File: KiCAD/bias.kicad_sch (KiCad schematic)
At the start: 23 parts, among them Q2 2N7000, Q3 2N7000, U10 OPA454, U11 LM4040LP-5, U5 OPA454, U9 LM7805_TO220

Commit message: kicad(bias): swap C17/C18 from Device:C_Polarized to Device:C
1 uF X7R ceramic is non-polarized in production. The polarized symbol
was an assembly-orientation hazard for a part that doesn't actually
have polarity. Pin numbers and connections unchanged.

- lib_id Device:C_Polarized -> Device:C on both caps
- Description property "Polarized capacitor" -> "Unpolarized capacitor"
- grid_bias.md: update note and check off the open-item

Co-Authored-By: Claude Opus 4.7 <noreply@anthropic.com>
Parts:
- C17, C18: symbol Device:C_Polarized -> Device:C
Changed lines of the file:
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@@
 	)
 	(symbol
-		(lib_id "Device:C_Polarized")
+		(lib_id "Device:C")
 		(at 107.95 163.83 0)
 		(unit 1)
@@
 			)
 		)
-		(property "Description" "Polarized capacitor"
+		(property "Description" "Unpolarized capacitor"
 			(at 107.95 163.83 0)
 			(hide yes)
@@
 	)
 	(symbol
-		(lib_id "Device:C_Polarized")
+		(lib_id "Device:C")
 		(at 107.95 185.42 0)
 		(unit 1)
@@
 			)
 		)
-		(property "Description" "Polarized capacitor"
+		(property "Description" "Unpolarized capacitor"
 			(at 107.95 185.42 0)
 			(hide yes)

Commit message: kicad: assign 1/4 W metal-film through-hole footprint to all resistors
Footprint: Resistor_THT:R_Axial_DIN0207_L6.3mm_D2.5mm_P10.16mm_Horizontal

DIN 0207 is the standard 1/4 W metal-film body size (Vishay MRS25, Yageo
MFR-25, etc., 6.3 mm x 2.5 mm). The relaxed P10.16mm pitch (vs the snug
P7.62mm) gives extra lead-bend room for hand soldering.

- bias.kicad_sch: 10 resistors (R_FA, R_FB, R_GA, R_GB, R_GATE, R_GLA,
  R_GLB, R_PADA, R_PADB, R_Z)
- buffer_keyer.kicad_sch: 25 resistors (R1-R16, RF_OP, RF_OP1, RG_OP,
  RG_OP1, RLA, RLB, R_INJ1, R_INJ2, Re)

All values fit comfortably in the DIN 0207 body, including the three
51-ohm MC1496 emitter resistors (1 % metal film for carrier-null
precision) and the 330 k MCP4728 null-injection isolators.

Co-Authored-By: Claude Opus 4.7 <noreply@anthropic.com>
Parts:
- R_FA, R_FB, R_GA, R_GATE, R_GB, R_GLA, R_GLB, R_PADA, R_PADB, R_Z: footprint (none) -> Resistor_THT:R_Axial_DIN0207_L6.3mm_D2.5mm_P10.16mm_Horizontal
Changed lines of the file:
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@@
 			)
 		)
-		(property "Footprint" ""
+		(property "Footprint" "Resistor_THT:R_Axial_DIN0207_L6.3mm_D2.5mm_P10.16mm_Horizontal"
 			(at 72.644 77.724 90)
 			(hide yes)
@@
 			)
 		)
-		(property "Footprint" ""
+		(property "Footprint" "Resistor_THT:R_Axial_DIN0207_L6.3mm_D2.5mm_P10.16mm_Horizontal"
 			(at 73.914 85.344 90)
 			(hide yes)
@@
 			)
 		)
-		(property "Footprint" ""
+		(property "Footprint" "Resistor_THT:R_Axial_DIN0207_L6.3mm_D2.5mm_P10.16mm_Horizontal"
 			(at 105.664 120.904 90)
 			(hide yes)
@@
 			)
 		)
-		(property "Footprint" ""
+		(property "Footprint" "Resistor_THT:R_Axial_DIN0207_L6.3mm_D2.5mm_P10.16mm_Horizontal"
 			(at 71.374 124.714 90)
 			(hide yes)
@@
 			)
 		)
-		(property "Footprint" ""
+		(property "Footprint" "Resistor_THT:R_Axial_DIN0207_L6.3mm_D2.5mm_P10.16mm_Horizontal"
 			(at 105.664 81.534 90)
 			(hide yes)
@@
 			)
 		)
-		(property "Footprint" ""
+		(property "Footprint" "Resistor_THT:R_Axial_DIN0207_L6.3mm_D2.5mm_P10.16mm_Horizontal"
 			(at 89.154 68.834 90)
 			(hide yes)
@@
 			)
 		)
-		(property "Footprint" ""
+		(property "Footprint" "Resistor_THT:R_Axial_DIN0207_L6.3mm_D2.5mm_P10.16mm_Horizontal"
 			(at 92.964 108.204 90)
 			(hide yes)
@@
 			)
 		)
-		(property "Footprint" ""
+		(property "Footprint" "Resistor_THT:R_Axial_DIN0207_L6.3mm_D2.5mm_P10.16mm_Horizontal"
 			(at 54.864 131.064 90)
 			(hide yes)
@@
 			)
 		)
-		(property "Footprint" ""
+		(property "Footprint" "Resistor_THT:R_Axial_DIN0207_L6.3mm_D2.5mm_P10.16mm_Horizontal"
 			(at 39.116 114.554 90)
 			(hide yes)
@@
 			)
 		)
-		(property "Footprint" ""
+		(property "Footprint" "Resistor_THT:R_Axial_DIN0207_L6.3mm_D2.5mm_P10.16mm_Horizontal"
 			(at 77.724 117.094 90)
 			(hide yes)

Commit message: docs+kicad+qucs: lock in cathode-monitor diode-OR design
KiCad bias sheet: fill in placeholder R values for the cathode-monitor
section -- R18=10K (threshold divider bottom), R20=R22=7.5K (R_SOURCE,
one per channel), R21=R23=470K (R_HYST, one per channel). All cathode-
monitor resistors now match the QUCS test bench values.

QUCS grid_bias_check.sch: rebuild test bench with LM393-equivalent
behavioral comparator (gain 1e4 to avoid the 1e6 convergence trap),
R_HYST=470K, R_SOURCE=7.5K, sweep input V2 against threshold V3=1.0V.
Sweep crosses the trip point cleanly with the lower gain.

pa_cathode_monitor.md: lock in the diode-OR combiner topology (no
inverter) chosen this session. Corrects the prior wired-OR description
which had the wrong polarity for an OC-direct-tie scheme. Updates:
  - Level 5 table: add R_SOURCE row, mark R_PULLUP as per-channel
  - Level 5 narrative: corrects input polarity (V_sense on +, threshold
    on -, fault=HIGH) and timing budget
  - Threshold divider: R17/RV1/R18 = 27K/10K/10K giving 1.06-2.13V
    wiper range (was an older 4.7K/1K/1.5K plan)
  - Per-tube summing: explicit diode-OR diagram with rationale for why
    a naive wired-tie gives wired-AND-of-fault instead of OR
  - Watchdog gate: replace stale screen-voltage interrupter section
    with grid-bias slam (Q2/Q3 on bias sheet) pointer
  - BOM: updated to match
  - Open items: latch decision resolved; new items track diode-OR
    parts (D_OR_A/B, R_PD) and I_CATHODE_A/B labels still to add

Add 1N5817 and Bourns 3296W trim-pot datasheets used for these decisions.

Co-Authored-By: Claude Opus 4.7 <noreply@anthropic.com>
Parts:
- added C24, C27, C31: 100nF, symbol Device:C
- added C25, C26, C30: 10uF, symbol Device:C_Polarized
- added C28, C29: 1nF, symbol Device:C
- added D1, D2, D3, D4: 1N5817, Diode_THT:D_DO-41_SOD81_P10.16mm_Horizontal, symbol Diode:1N5817
- added R17: 27K, symbol Device:R_US
- added R18: 10K, symbol Device:R_US
- added R19: 4.7K, symbol Device:R_US
- added R20, R22: 7.5K, symbol Device:R_US
- added R21, R23: 470K, symbol Device:R_US
- added RV1: 10K, symbol Device:R_Potentiometer_US
- added U12: LM393, symbol Comparator:LM393
- added U13, U14: OPA1641, symbol Amplifier_Operational:OPA1641
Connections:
- net +5V: now also C24.1, C25.1, C26.1, C27.1, C30.1, C31.1, U12.8 (V+), U13.7 (V+), U14.7 (V+)
- net GND: now also C24.2, C25.2, C26.2, C27.2, C28.2, C29.2, C30.2, C31.2, D1.2 (A), D3.2 (A), R18.2, U12.4 (V-), U13.4 (V-), U14.4 (V-)
- net GRID_BLOCK_CRASH: now also R19.2, R21.2, R23.2, U12.1, U12.7
- net +5V_REF: now reaches C23.1, R_GA.1, R_GB.1, R_Z.2, U11.2 (K)
- net +5V_REF: now also R17.1
- new net: R18.1, RV1.3
- new net: R20.1, U13.2 (-), U13.6
- new net: R20.2, R21.1, U12.5 (+)
- new net: R22.1, U14.2 (-), U14.6
- new net: R22.2, R23.1, U12.3 (+)
- new net: R17.2, RV1.1
- new net: RV1.2, U12.2 (-), U12.6 (-)
- new net +3.3V: D2.1 (K), D4.1 (K), R19.1
- new net CATHODE_SENSE_A: C29.1, D3.1 (K), D4.2 (A), U14.3 (+)
- new net CATHODE_SENSE_B: C28.1, D1.1 (K), D2.2 (A), U13.3 (+)

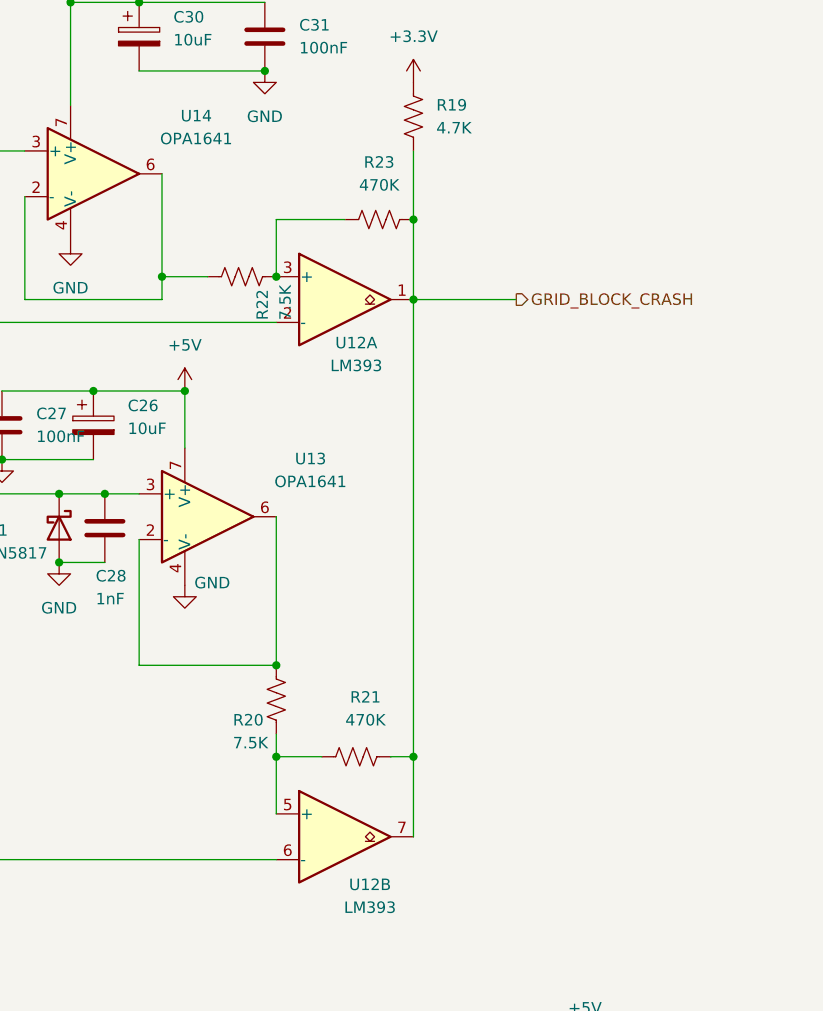
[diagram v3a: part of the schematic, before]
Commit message: kicad+pdf+tools: diode-OR build-out, cap footprints, regen monitor PDF
KiCad bias sheet: complete the cathode-monitor diode-OR combiner
  - D5, D6 = 1N4148 (diode-OR anodes at each LM393 OC output)
  - R24 = 100 kOhm (R_PD pulldown at common GRID_BLOCK_CRASH node)
  - R25 = 4.7 kOhm (second R_PULL so each LM393 OC has its own
    pull-up to +3.3 V, satisfying the diode-OR topology)
  - Closes the "remaining bias-sheet work" item from the cathode-
    monitor spec's open list.

KiCad arduino sheet: add I_CATHODE_A and I_CATHODE_B hierarchical
inputs so the ADC1 path from the bias sheet has a landing point on
the Metro side.

Tools: add assign_cap_footprints.py, a re-runnable script that walks
.kicad_sch files and assigns THT capacitor footprints by value, based
on the parts on the 2026-06-19 Mouser order:
  100nF / 0.1uF  KEMET C410   C_Disc_D5.0mm_W2.5mm_P5.00mm
  10uF           Panasonic    CP_Radial_D5.0mm_P2.00mm
  680nF / 0.68uF WIMA MKP4    C_Rect_L13.0mm_W6.0mm_P10.00mm_FKS3_FKP3_MKS4
  10nF / 0.01uF  Vishay Y5P   C_Disc_D6.0mm_W2.5mm_P5.00mm
  220pF          Knowles mica C_Rect_L7.0mm_W4.5mm_P5.00mm
Only fills empty Footprint fields; never overwrites. Preserves LF
line endings and writes UTF-8 without BOM (KiCad 10 treats a BOM-
prefixed .kicad_sch as empty).

Run output: 10 caps updated on bias sheet, 17 on buffer_keyer sheet.
Values still needing the user to measure (not in this order):
  bias: C17/C18 1uF, C21 0.22uF, C28/C29 1nF
  buffer_keyer: C1 330pF, C13/C14/C15 1uF
  vfo: CF3/CF5 390pF

Cathode_Monitor_Schematic.pdf regenerated with the diode-OR topology
locked in:
  - Schematic page adds L5b diode-OR sub-diagram (D_OR_A horizontal,
    D_OR_B from "Ch. B" annotation, R_PD pulldown, GRID_BLOCK_CRASH
    output)
  - R_SOURCE now drawn explicitly between OPA1641 OUT and LM393 (+)
  - V_REF block replaced with V_THR (R17/RV1/R18 trim, 1.06-2.13 V)
  - BOM, layers table, operating-points action column updated
  - "Watchdog gate" section rewritten: bias s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
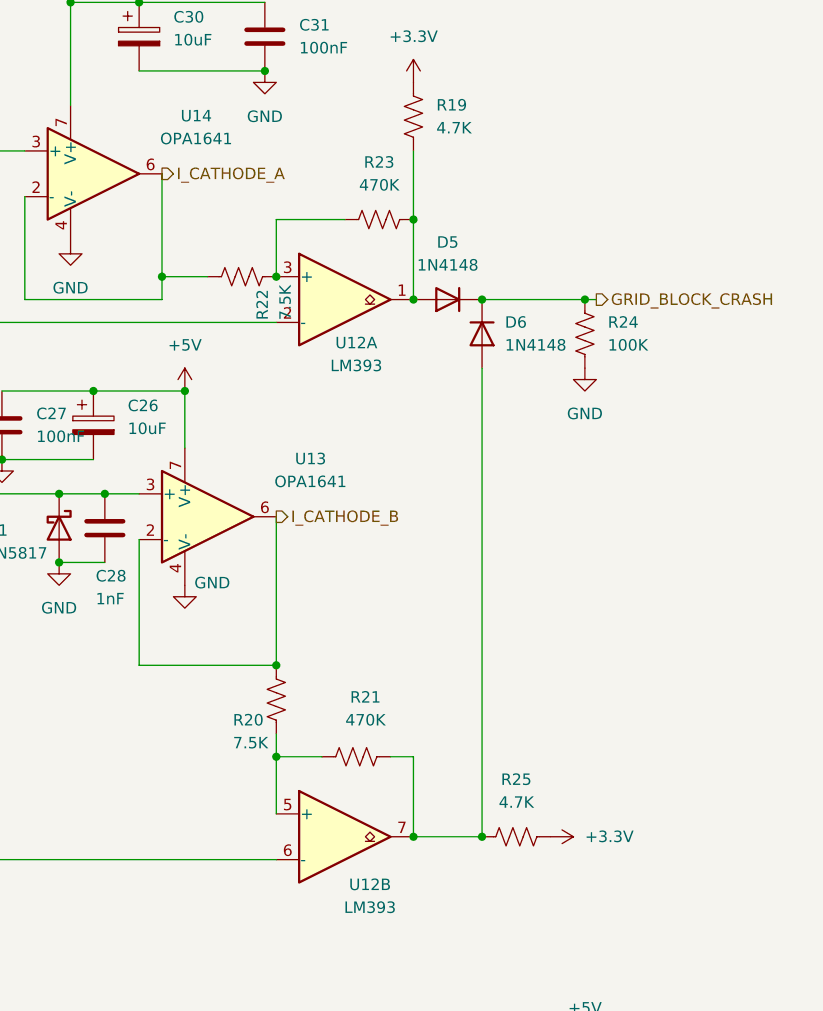
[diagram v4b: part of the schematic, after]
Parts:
- added D5, D6: 1N4148, Diode_THT:D_DO-35_SOD27_P7.62mm_Horizontal, symbol Diode:1N4148
- added R24: 100K, symbol Device:R_US
- added R25: 4.7K, symbol Device:R_US
- C19, C20, C22, C23, C24, C27, C31: footprint (none) -> Capacitor_THT:C_Disc_D5.0mm_W2.5mm_P5.00mm
- C25, C26, C30: footprint (none) -> Capacitor_THT:CP_Radial_D5.0mm_P2.00mm
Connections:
- net +3.3V: now also R25.2
- net GND: now also R24.2
- net GRID_BLOCK_CRASH: now also D5.1 (K), D6.1 (K), R24.1; no longer R19.2, R21.2, R23.2, U12.1, U12.7
- net I_CATHODE_B: now reaches R20.1, U13.2 (-), U13.6
- net I_CATHODE_A: now reaches R22.1, U14.2 (-), U14.6
- new net: D5.2 (A), R19.2, R23.2, U12.1
- new net: D6.2 (A), R21.2, R25.1, U12.7

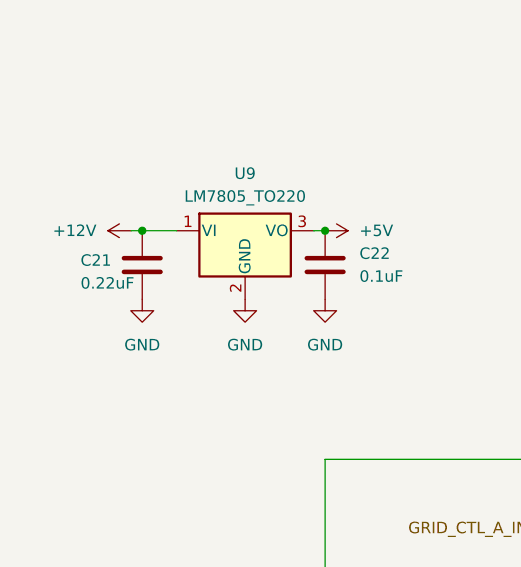
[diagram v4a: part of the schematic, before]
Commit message: caps: complete footprint coverage on active sheets + add datasheets
Pending Mouser cart 2026-06-24 (1:31 PM) adds two more KEMET parts
that close the remaining cap gaps:

  KEMET C317C334K3R5TA  0.33 uF X7R  25V  LS=5.08mm  (qty 4)
  KEMET C327C102J3G5TA  1000 pF C0G  25V  LS=5.08mm  (qty 5)

Updated VALUE_TO_FOOTPRINT and re-ran the script:
  bias: C21 0.33uF -> C_Rect_L7.0mm_W3.5mm_P5.00mm
  bias: C28/C29 1nF -> C_Rect_L7.0mm_W3.5mm_P5.00mm

Every capacitor across the active sheets (bias, buffer_keyer, vfo,
arduino) now has a footprint assigned. The 100pF (AVX AR21) mapping
remains for future PA tank / LPF use; no current schematic instance.

Also: Documentation/Components/ added for traceability of part choices:
  90968303_1-3748A_2026-06-19.pdf  -- Mouser invoice (R/Q/LM7171/DAC/etc)
  AR-Series.pdf                    -- AVX SkyCap/AR series MLCC
  C330C105K2R5TA.pdf               -- KEMET 1uF X7R 200V datasheet
  KEM_C1049_GOLDMAX_C0G.pdf        -- KEMET GoldMax C0G series
  KEM_C1050_GOLDMAX_X7R.pdf        -- KEMET GoldMax X7R series

Co-Authored-By: Claude Opus 4.7 <noreply@anthropic.com>
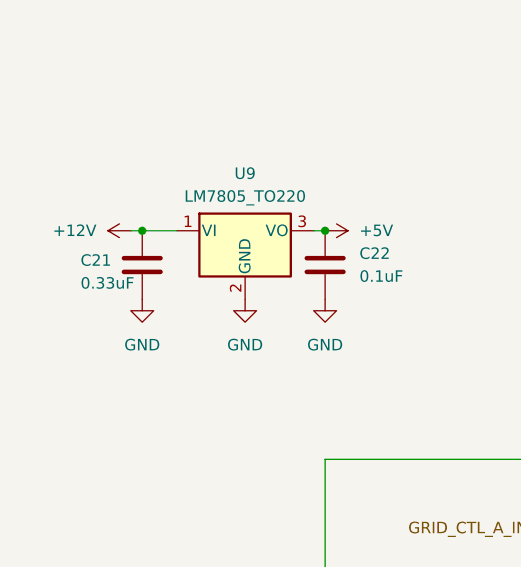
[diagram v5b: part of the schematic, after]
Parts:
- C17, C18: footprint (none) -> Capacitor_THT:C_Rect_L7.2mm_W4.5mm_P5.00mm
- C21: value 0.22uF -> 0.33uF; footprint (none) -> Capacitor_THT:C_Rect_L7.0mm_W3.5mm_P5.00mm
- C28, C29: footprint (none) -> Capacitor_THT:C_Rect_L7.0mm_W3.5mm_P5.00mm
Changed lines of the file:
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@@
 			)
 		)
-		(property "Value" "0.22uF"
+		(property "Value" "0.33uF"
 			(at 18.542 59.182 0)
 			(show_name no)
@@
 			)
 		)
-		(property "Footprint" ""
+		(property "Footprint" "Capacitor_THT:C_Rect_L7.0mm_W3.5mm_P5.00mm"
 			(at 26.3652 60.96 0)
 			(hide yes)
@@
 			)
 		)
-		(property "Footprint" ""
+		(property "Footprint" "Capacitor_THT:C_Rect_L7.2mm_W4.5mm_P5.00mm"
 			(at 108.9152 167.64 0)
 			(hide yes)
@@
 			)
 		)
-		(property "Footprint" ""
+		(property "Footprint" "Capacitor_THT:C_Rect_L7.0mm_W3.5mm_P5.00mm"
 			(at 205.4352 86.36 0)
 			(hide yes)
@@
 			)
 		)
-		(property "Footprint" ""
+		(property "Footprint" "Capacitor_THT:C_Rect_L7.2mm_W4.5mm_P5.00mm"
 			(at 108.9152 189.23 0)
 			(hide yes)
@@
 			)
 		)
-		(property "Footprint" ""
+		(property "Footprint" "Capacitor_THT:C_Rect_L7.0mm_W3.5mm_P5.00mm"
 			(at 190.1952 48.26 0)
 			(hide yes)

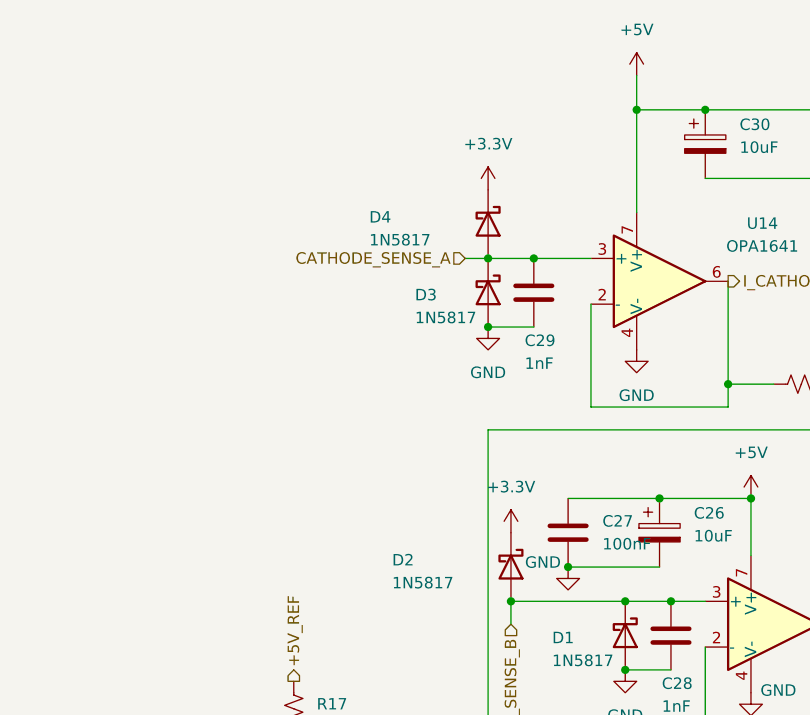
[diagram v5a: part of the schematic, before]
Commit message: kicad/bias: footprint cleanup -- D2/D4 +3.3V bulk + remaining cathode-monitor parts
User added two ECA-1EM100 10uF electrolytics for the D2/D4 fault-energy
absorption requirement, plus all the cathode-monitor section parts were
still missing footprints from when they were added.

Footprints assigned:
  C32, C33 -- 10uF (ECA-1EM100) -> CP_Radial_D5.0mm_P2.00mm
              (auto-assigned by assign_cap_footprints.py)
  R17-R25  -- 9x 1/4W metal-film -> R_Axial_DIN0207_L6.3mm_D2.5mm_P10.16mm_Horizontal
  RV1      -- 10K 25-turn cermet -> Potentiometer_Bourns_3296W_Vertical
  U12      -- LM393 dual comparator -> DIP-8_W7.62mm (Mill-Max 8P socket)
  U13, U14 -- OPA1641 -> DIP-8_W7.62mm (SOIC-to-DIP adapter into 8P socket)

C32 and C33 wiring verified:
  C32 (+ pin) -> +3.3V at (184.15, 33.02); (- pin) -> GND at (165.10, 33.02)
                 channel A, near D4 clamp
  C33 (+ pin) -> +3.3V at (186.69, 71.12); (- pin) -> GND at (175.26, 71.12)
                 channel B, near D2 clamp
Both polarized correctly for electrolytic; rail correctly identified as +3.3V.

Diode-OR wiring also verified:
  D5 anode (238.76, 57.15) = U12 ch A OC, cathode (246.38, 57.15) at common
  D6 anode (246.38, 64.77) connects to U12 ch B OC (238.76, 116.84) via long
           routing wire (south 52mm, then west 7.6mm)
  R19, R25 = per-channel 4.7K pull-ups to +3.3V
  R24 = 100K pull-down between common node and GND
  GRID_BLOCK_CRASH label tapped on the common node

Co-Authored-By: Claude Opus 4.7 <noreply@anthropic.com>
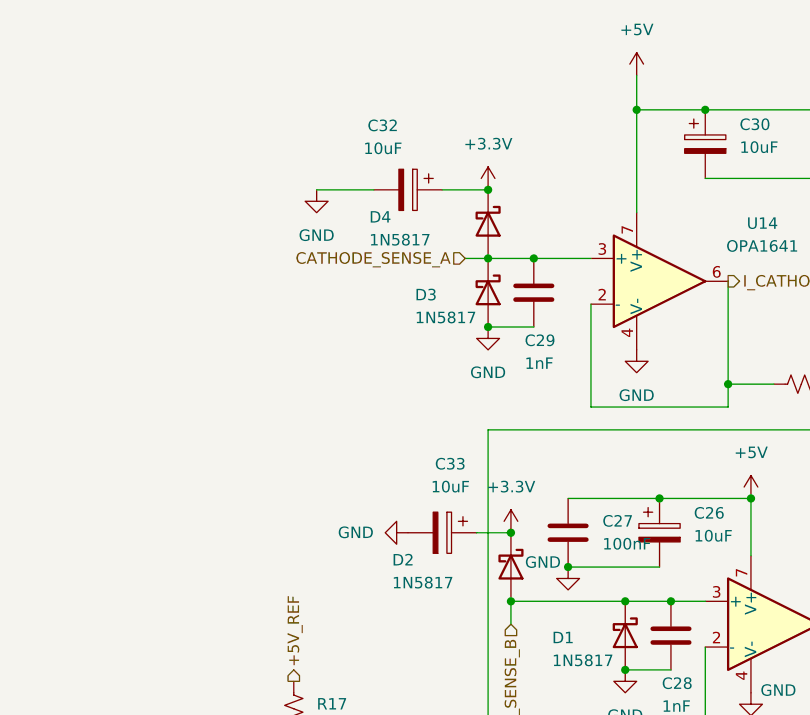
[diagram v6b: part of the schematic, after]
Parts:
- added C32, C33: 10uF, Capacitor_THT:CP_Radial_D5.0mm_P2.00mm, symbol Device:C_Polarized
- R17, R18, R19, R20, R21, R22, R23, R24, R25: footprint (none) -> Resistor_THT:R_Axial_DIN0207_L6.3mm_D2.5mm_P10.16mm_Horizontal
- RV1: footprint (none) -> Potentiometer_THT:Potentiometer_Bourns_3296W_Vertical
- U12, U13, U14: footprint (none) -> Package_DIP:DIP-8_W7.62mm
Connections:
- net +3.3V: now also C32.1, C33.1
- net GND: now also C32.2, C33.2
